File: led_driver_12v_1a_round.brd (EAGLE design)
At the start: 32 x 32 mm, 54 parts, among them Q1 BSZ0902NSI, Q2 BSZ0902NSI, Q3 BSZ0902NSI, Q4 BSZ0902NSI, Q5 BSZ0902NSI, Q6 SSM3K2615R

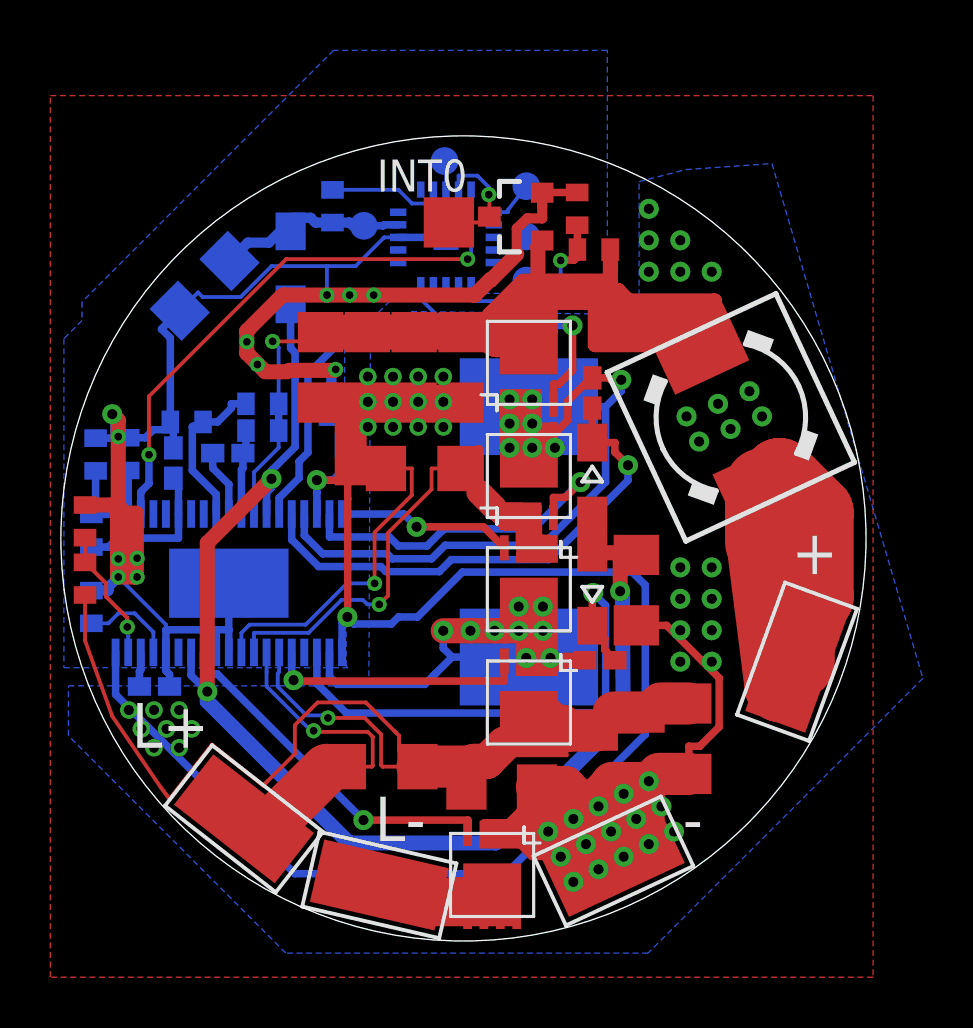
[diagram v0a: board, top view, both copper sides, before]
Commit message: added vias for led in roud version, added second button pad in round version
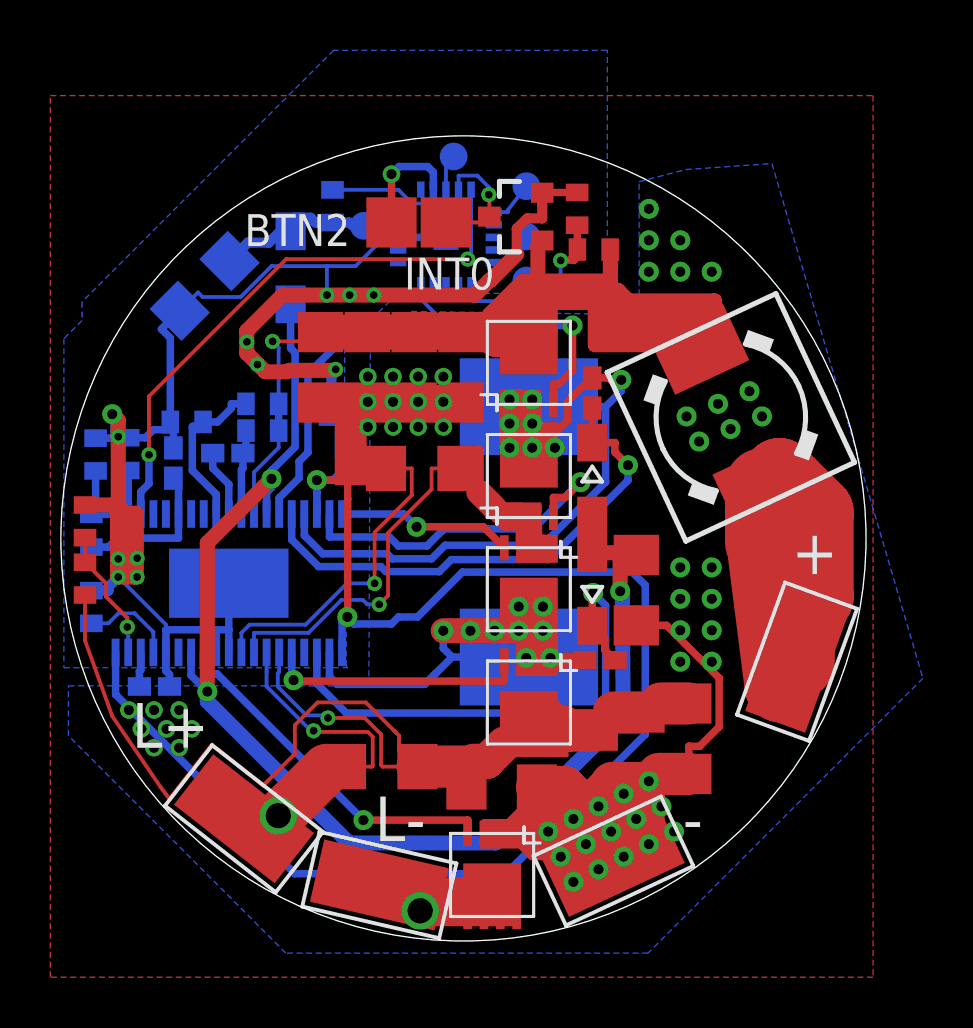
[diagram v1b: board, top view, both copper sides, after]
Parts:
- added BTN2: TPTP20SQ, testpad:TP20SQ
- moved RST 0.40 mm to (15.6, 31.2)
- moved INT0 0.12 mm to (15.3, 28.6)
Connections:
- new net N$8: BTN2.TP, U$2.12
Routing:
- net N$8: track 0.00 -> 4.49 mm, vias 0 -> 1
- net ISN: track 13.9 -> 14.9 mm, vias 1 -> 2
- net N$19: track 26.1 -> 26.5 mm, vias 0 -> 1
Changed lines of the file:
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@@
 <attribute name="TP_SIGNAL_NAME" value="" x="20.405" y="30" size="1" layer="38" rot="MR270"/>
 </element>
-<element name="RST" library="testpad" package="TP11R" value="TPTP11R" x="15.25" y="31" smashed="yes" rot="MR270">
-<attribute name="TP_SIGNAL_NAME" value="" x="17.155" y="31" size="1" layer="38" rot="MR270"/>
+<element name="RST" library="testpad" package="TP11R" value="TPTP11R" x="15.61" y="31.18" smashed="yes" rot="MR270">
+<attribute name="TP_SIGNAL_NAME" value="" x="17.515" y="31.18" size="1" layer="38" rot="MR270"/>
 </element>
 <element name="VCC" library="testpad" package="TP11R" value="TPTP11R" x="12.04" y="28.425" smashed="yes" rot="MR270">
 <attribute name="TP_SIGNAL_NAME" value="" x="13.945" y="28.425" size="1" layer="38" rot="MR270"/>
 </element>
-<element name="INT0" library="testpad" package="TP20SQ" value="TPTP20SQ" x="15.42" y="28.56" smashed="yes">
-<attribute name="TP_SIGNAL_NAME" value="" x="15.42" y="26.02" size="1" layer="37"/>
-<attribute name="NAME" x="12.56" y="29.79" size="1.27" layer="25"/>
-<attribute name="VALUE" x="14.404" y="27.417" size="0.0254" layer="27"/>
+<element name="INT0" library="testpad" package="TP20SQ" value="TPTP20SQ" x="15.3" y="28.56" smashed="yes">
+<attribute name="TP_SIGNAL_NAME" value="" x="15.3" y="26.02" size="1" layer="37"/>
+<attribute name="NAME" x="13.64" y="25.89" size="1.27" layer="25"/>
+<attribute name="VALUE" x="14.284" y="27.417" size="0.0254" layer="27"/>
+</element>
+<element name="BTN2" library="testpad" package="TP20SQ" value="TPTP20SQ" x="13.14" y="28.56" smashed="yes" rot="R90">
+<attribute name="TP_SIGNAL_NAME" value="" x="15.68" y="28.56" size="1" layer="37" rot="R90"/>
+<attribute name="NAME" x="11.5" y="28.89" size="1.27" layer="25" rot="R180"/>
+<attribute name="VALUE" x="14.283" y="27.544" size="0.0254" layer="27" rot="R90"/>
 </element>
 </elements>
@@
 <via x="10.0437" y="8.35695" extent="1-16" drill="0.3048" diameter="0.6096"/>
 <wire x1="8.175" y1="11.47" x2="8.175" y2="10.691390625" width="0.1524" layer="16"/>
-<wire x1="7.278434375" y1="4.856990625" x2="8.03635" y2="4.31635" width="2" layer="1"/>
+<wire x1="7.278434375" y1="4.856990625" x2="7.9461125" y2="4.38071875" width="2" layer="1"/>
+<wire x1="7.9461125" y1="4.38071875" x2="8.03635" y2="4.31635" width="2" layer="1"/>
 <wire x1="8.03635" y1="4.31635" x2="10.56" y2="6.84" width="2" layer="1"/>
 <wire x1="11.328" y1="6.93" x2="10.65" y2="6.93" width="1" layer="1"/>
 <wire x1="10.65" y1="6.93" x2="10.56" y2="6.84" width="1" layer="1"/>
+<via x="8.64" y="4.98" extent="1-16" drill="1"/>
+<wire x1="8.64" y1="4.98" x2="8.54539375" y2="4.98" width="0.4064" layer="1"/>
+<wire x1="8.54539375" y1="4.98" x2="7.9461125" y2="4.38071875" width="0.4064" layer="1"/>
 </signal>
 <signal name="ISP">
@@
 <via x="17.00713125" y="29.66423125" extent="1-16" drill="0.3048" diameter="0.6096"/>
 <contactref element="INT0" pad="TP"/>
-<wire x1="15.42" y1="28.56" x2="16.8" y2="28.56" width="0.16" layer="1"/>
+<wire x1="15.3" y1="28.56" x2="16.8" y2="28.56" width="0.16" layer="1"/>
 <wire x1="16.8" y1="28.56" x2="17.03" y2="28.79" width="0.16" layer="1"/>
 </signal>
@@
 <contactref element="RST" pad="TP"/>
 <wire x1="15.305" y1="29.865" x2="15.305" y2="30.99" width="0.1524" layer="16"/>
-<wire x1="15.305" y1="30.99" x2="15.25" y2="31" width="0.1524" layer="16"/>
+<wire x1="15.305" y1="30.99" x2="15.61" y2="31.18" width="0.1524" layer="16"/>
 </signal>
 <signal name="N$20">
@@
 <wire x1="17.7" y1="1.02" x2="17.7" y2="1.14" width="0.1524" layer="1"/>
 <wire x1="17.7" y1="1.14" x2="17.465" y2="0.975" width="0.1524" layer="1"/>
+<via x="14.28" y="1.2" extent="1-16" drill="1"/>
+<wire x1="14.28" y1="1.2" x2="14.28" y2="0.96" width="0.4064" layer="1"/>
+<wire x1="14.28" y1="0.96" x2="14.4" y2="0.84" width="0.4064" layer="1"/>
 </signal>
 <signal name="N$21">
@@
 <wire x1="29.258090625" y1="12.878090625" x2="29.258090625" y2="11.099709375" width="3" layer="1"/>
 </signal>
+<signal name="N$8">
+<contactref element="U$2" pad="12"/>
+<contactref element="BTN2" pad="TP"/>
+<wire x1="14.805" y1="29.865" x2="14.805" y2="30.555" width="0.3" layer="16"/>
+<wire x1="14.805" y1="30.555" x2="14.58" y2="30.78" width="0.3" layer="16"/>
+<wire x1="14.58" y1="30.78" x2="13.44" y2="30.78" width="0.3" layer="16"/>
+<wire x1="13.44" y1="30.78" x2="13.14" y2="30.48" width="0.3" layer="16"/>
+<via x="13.14" y="30.48" extent="1-16" drill="0.4"/>
+<wire x1="13.14" y1="30.48" x2="13.14" y2="28.56" width="0.3" layer="1"/>
+</signal>
 </signals>
